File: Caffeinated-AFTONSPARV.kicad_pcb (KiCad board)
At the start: 4 copper layers, 42.5 x 16.1 mm, 37 parts, among them J1 PWR, J2 LED, J3 TagConnect, J4 USB, Q1 AO3400A, Q2 AO3400A, Q3 AO3400A, SW1 SW_Push, U1 ESP32-C3-MINI-1-[H/N]4, U2 SY8201ABC

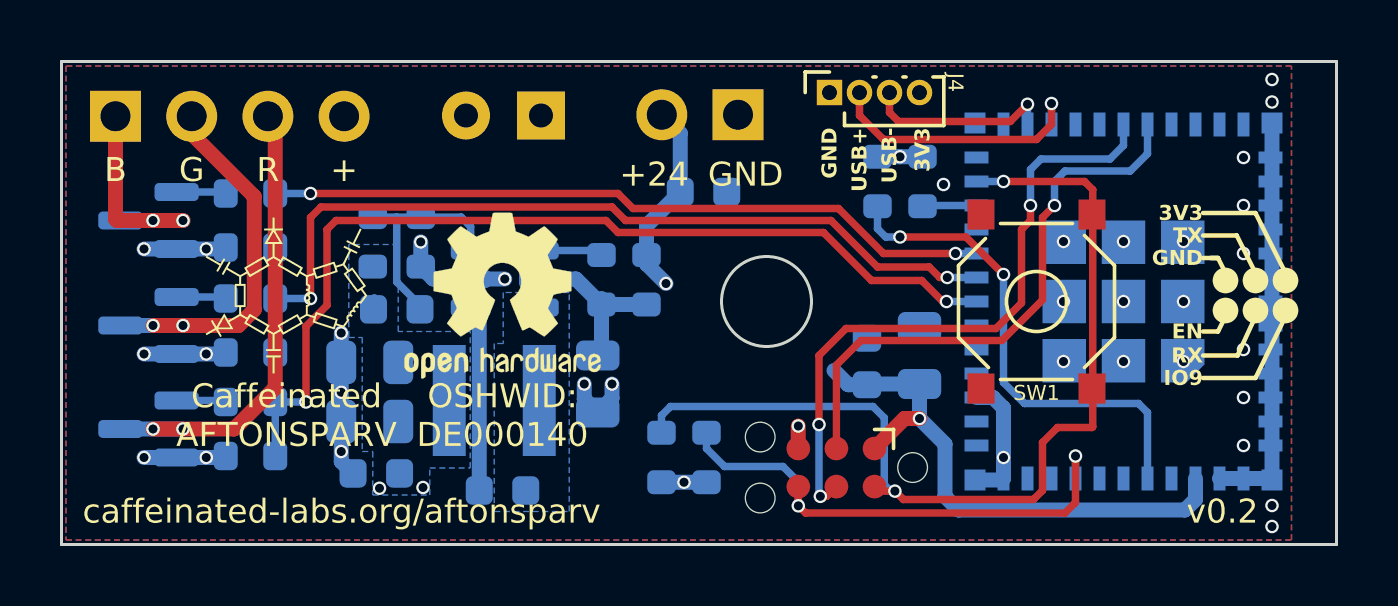
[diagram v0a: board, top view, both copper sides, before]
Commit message: Added JST SH 4P
Added JST SH 4P connector for UART flashing, to schematic and PCB, and rerouted traces and components to make that happen
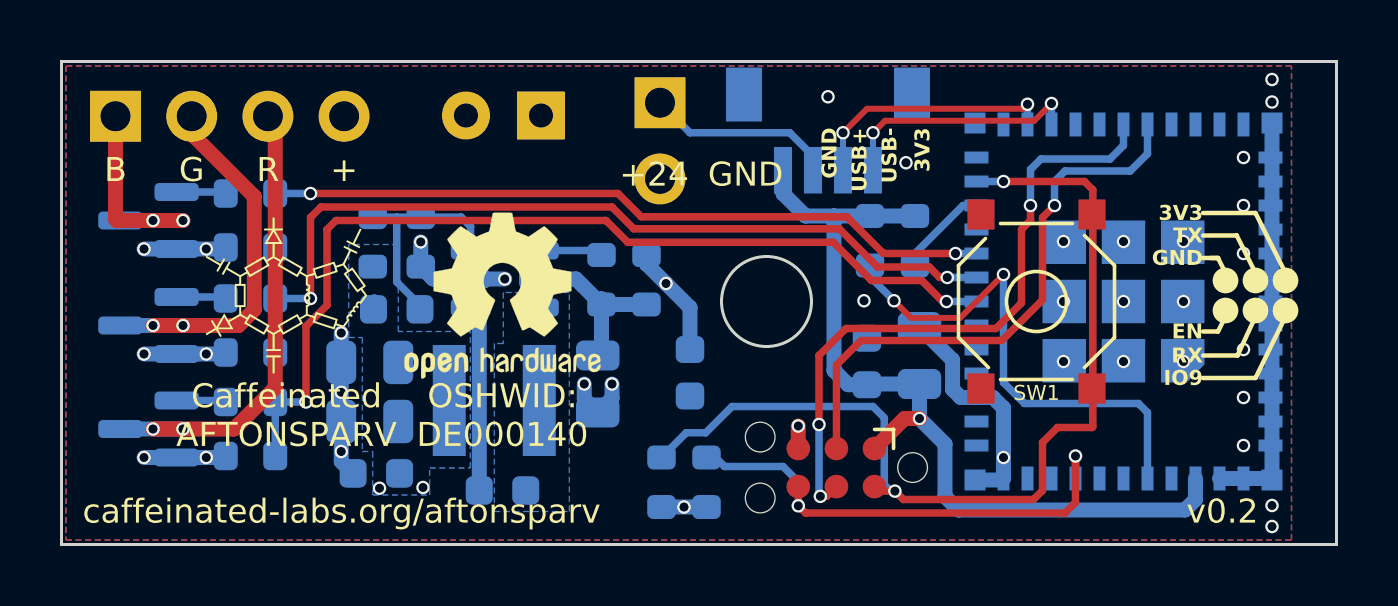
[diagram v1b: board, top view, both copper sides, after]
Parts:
- J4: footprint Connector_PinSocket_1.00mm:PinSocket_1x04_P1.00mm_Vertical -> JST_SH_BM04B-SRSS-TB_LF__SN__KiCad:BM04B-SRSS-TB_LFSN_; moved to B.Cu
- moved C1 6.04 mm to (150.8, 102.4), turned to -90 degrees
- moved J4 3.64 mm to (158.3, 95.2), turned to 180 degrees
- moved J1 2.63 mm to (149.8, 93.4), turned to 180 degrees
- moved R8 1.99 mm to (156.8, 98.0)
- moved R9 1.99 mm to (158.2, 98.0)
- moved R10 0.83 mm to (151.3, 106.0)
- moved R7 0.83 mm to (149.8, 106.0)
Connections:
- J4 pad 1: GND -> USB-D+
- J4 pad 2: USB-D+ -> USB-D-
- J4 pad 3: USB-D- -> GND
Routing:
- net GND: track 37.9 -> 47.6 mm, vias 36 -> 38
- net +3.3V: track 21.3 -> 30.4 mm, vias 5 -> 4
- net +24V: track 6.61 -> 3.79 mm
- net USB-D-: track 6.30 -> 8.61 mm, vias 1 -> 2
- net Net-(U1-GPIO8): track 1.93 -> 3.11 mm
- net USB-D+: track 9.10 -> 8.30 mm, vias 1 -> 2
- net EN: track 17.3 -> 16.6 mm
